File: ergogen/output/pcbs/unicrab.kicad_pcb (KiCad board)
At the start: 2 copper layers, 230 x 104.3 mm, 72 parts

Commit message: update the kicad file
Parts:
- moved T1 46.8 mm to (172.2, 111.0), turned to 0 degrees
- moved B1 38.6 mm to (159.2, 121.0), turned to 90 degrees
- moved JST1 28.3 mm to (187.2, 151.3), turned to -90 degrees
- moved MCU1 2.48 mm to (172.2, 126.4)
- moved D22 1.97 mm to (251.8, 104.1)
- moved D26 1.97 mm to (228.8, 87.7)
- moved S23 1.97 mm to (246.1, 82.8)
- moved S18 1.97 mm to (275.6, 123.1)
- moved S24 1.97 mm to (236.3, 115.7)
- moved D17 1.97 mm to (144.6, 166.3)
- moved S11 1.97 mm to (128.7, 108.6)
- moved D30 1.97 mm to (204.8, 137.2)
- moved D20 1.97 mm to (268.1, 95.1)
- moved D6 1.97 mm to (97.0, 87.7)
- moved D23 1.97 mm to (247.4, 87.7)
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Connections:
- T1 pad 1: pos -> RAW
- T1 pad 2: RAW -> pos
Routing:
- net P017: track 0.00 -> 21.6 mm
- net P008: track 0.00 -> 21.6 mm
- net P020: track 0.00 -> 21.6 mm
- net P029: track 0.00 -> 21.6 mm
- net P031: track 0.00 -> 21.6 mm
- net P006: track 0.00 -> 21.6 mm
- net P106: track 0.00 -> 8.92 mm
- net P009: track 0.00 -> 8.92 mm
- net mirror_tucky_cluster: track 0.00 -> 4.46 mm
- net mirror_reachy_cluster: track 0.00 -> 4.46 mm
- net tucky_cluster: track 0.00 -> 4.46 mm
- net reachy_cluster: track 0.00 -> 4.46 mm
- net mirror_index_top: track 0.00 -> 4.32 mm
- net mirror_ring_bottom: track 0.00 -> 4.32 mm
- net mirror_ring_home: track 0.00 -> 4.32 mm
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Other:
- board size 230 x 104.3 mm -> 230 x 103.8 mm
- net class Default removed

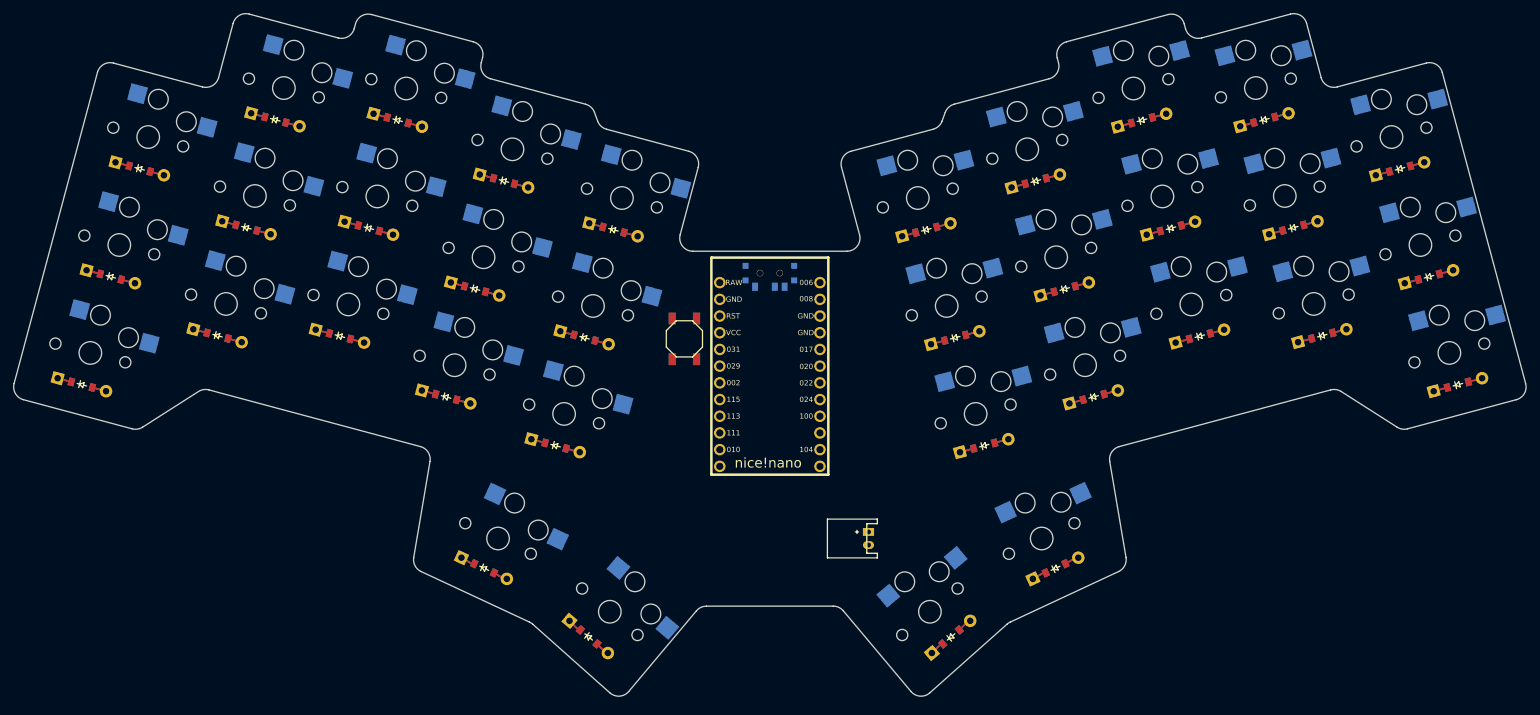
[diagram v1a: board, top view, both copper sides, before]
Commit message: add the pad to diode connections
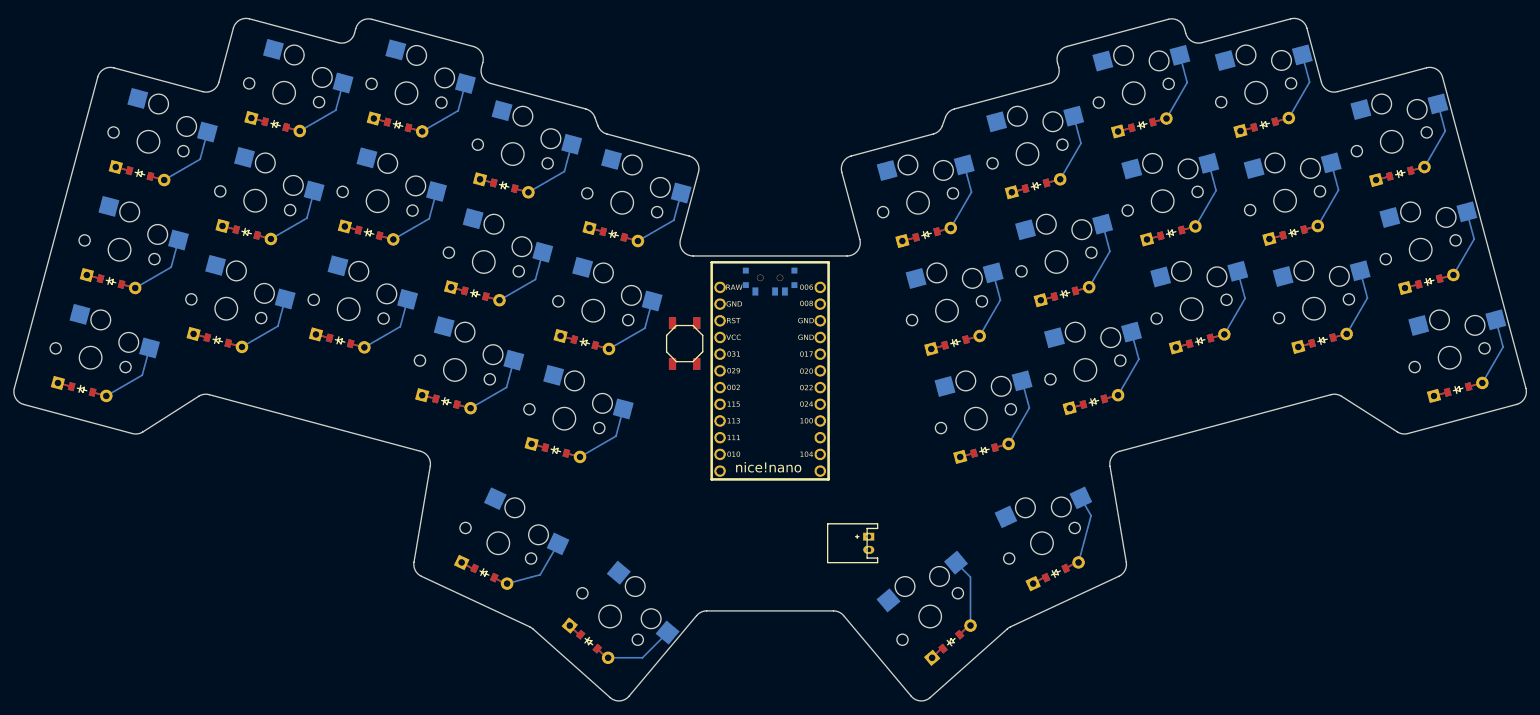
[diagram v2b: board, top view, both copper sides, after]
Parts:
- moved S23 0.72 mm to (246.2, 83.5)
- moved D32 0.72 mm to (196.0, 105.1)
- moved S18 0.72 mm to (275.6, 123.8)
- moved S20 0.72 mm to (266.8, 91.0)
- moved S2 0.72 mm to (73.3, 107.4)
- moved D33 0.72 mm to (215.7, 156.6)
- moved S33 0.72 mm to (213.6, 152.1)
- moved MCU1 0.72 mm to (172.2, 127.1)
- moved D19 0.72 mm to (272.5, 112.3)
- moved D28 0.72 mm to (217.1, 114.1)
- moved D20 0.72 mm to (268.1, 95.8)
- moved S14 0.72 mm to (145.3, 116.7)
- moved S15 0.72 mm to (149.7, 100.3)
- moved S32 0.72 mm to (194.7, 100.3)
- moved S9 0.72 mm to (116.9, 83.6)
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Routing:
- net tucky_cluster: track 4.46 -> 15.1 mm
- net reachy_cluster: track 4.46 -> 15.1 mm
- net inner_top: track 4.32 -> 14.9 mm
- net pinky_bottom: track 4.32 -> 14.9 mm
- net pinky_top: track 4.32 -> 14.9 mm
- net mirror_index_bottom: track 4.32 -> 14.9 mm
- net inner_home: track 4.32 -> 14.9 mm
- net ring_top: track 4.32 -> 14.9 mm
- net index_home: track 4.32 -> 14.9 mm
- net ring_bottom: track 4.32 -> 14.9 mm
- net index_bottom: track 4.32 -> 14.9 mm
- net middle_home: track 4.32 -> 14.9 mm
- net mirror_middle_bottom: track 4.32 -> 14.9 mm
- net middle_bottom: track 4.32 -> 14.9 mm
- net mirror_pinky_bottom: track 4.32 -> 14.9 mm
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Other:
- outline, holes or cut-outs redrawn

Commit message: connect rows and columns
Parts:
- moved D3 3.49 mm to (73.1, 97.0)
- moved S25 3.49 mm to (228.7, 101.2)
- moved D23 3.49 mm to (244.2, 89.5)
- moved D13 3.49 mm to (136.4, 139.1)
- moved S29 3.49 mm to (208.1, 94.0)
- moved S13 3.49 mm to (137.6, 134.3)
- moved D29 3.49 mm to (209.4, 98.8)
- moved S15 3.49 mm to (146.4, 101.4)
- moved D15 3.49 mm to (145.2, 106.2)
- moved D17 3.49 mm to (141.4, 168.2)
- moved D6 3.49 mm to (93.7, 89.5)
- moved S19 3.49 mm to (267.9, 108.6)
- moved D11 3.49 mm to (124.1, 115.3)
- moved D7 3.49 mm to (103.5, 122.4)
- moved D10 3.49 mm to (119.7, 131.7)
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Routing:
- net P002: track 0.00 -> 73.8 mm
- net P010: track 0.00 -> 73.8 mm
- net P115: track 0.00 -> 73.8 mm
- net P111: track 0.00 -> 73.8 mm
- net P113: track 0.00 -> 73.8 mm
- net P017: track 21.6 -> 95.3 mm
- net P008: track 21.6 -> 95.3 mm
- net P029: track 21.6 -> 95.3 mm
- net P006: track 21.6 -> 95.3 mm
- net P020: track 21.6 -> 95.3 mm
- net P031: track 21.6 -> 78.3 mm
- net P106: track 8.92 -> 27.6 mm
- net P009: track 8.92 -> 27.4 mm
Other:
- outline, holes or cut-outs redrawn

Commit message: add reset and switch connection
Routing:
- net GND: track 0.00 -> 14.6 mm
- net RST: track 0.00 -> 9.88 mm
- net RAW: track 0.00 -> 5.63 mm
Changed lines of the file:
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@@
 		(net 47)
 	)
+	(segment
+		(start 161.949416 114.91072)
+		(end 161.325164 114.286468)
+		(width 0.25)
+		(layer "B.Cu")
+		(net 48)
+	)
+	(segment
+		(start 166.695165 114.91072)
+		(end 161.949416 114.91072)
+		(width 0.25)
+		(layer "B.Cu")
+		(net 48)
+	)
+	(segment
+		(start 154.095161 119.73572)
+		(end 154.095161 125.935726)
+		(width 0.25)
+		(layer "F.Cu")
+		(net 50)
+	)
+	(segment
+		(start 157.004413 116.826468)
+		(end 161.325164 116.826468)
+		(width 0.25)
+		(layer "F.Cu")
+		(net 50)
+	)
+	(segment
+		(start 154.095161 119.73572)
+		(end 157.004413 116.826468)
+		(width 0.25)
+		(layer "F.Cu")
+		(net 50)
+	)
+	(segment
+		(start 160.955912 119.73572)
+		(end 161.325164 119.366468)
+		(width 0.25)
+		(layer "F.Cu")
+		(net 51)
+	)
+	(segment
+		(start 157.795161 119.73572)
+		(end 157.795161 125.935726)
+		(width 0.25)
+		(layer "F.Cu")
+		(net 51)
+	)
+	(segment
+		(start 157.795161 119.73572)
+		(end 160.955912 119.73572)
+		(width 0.25)
+		(layer "F.Cu")
+		(net 51)
+	)
 )

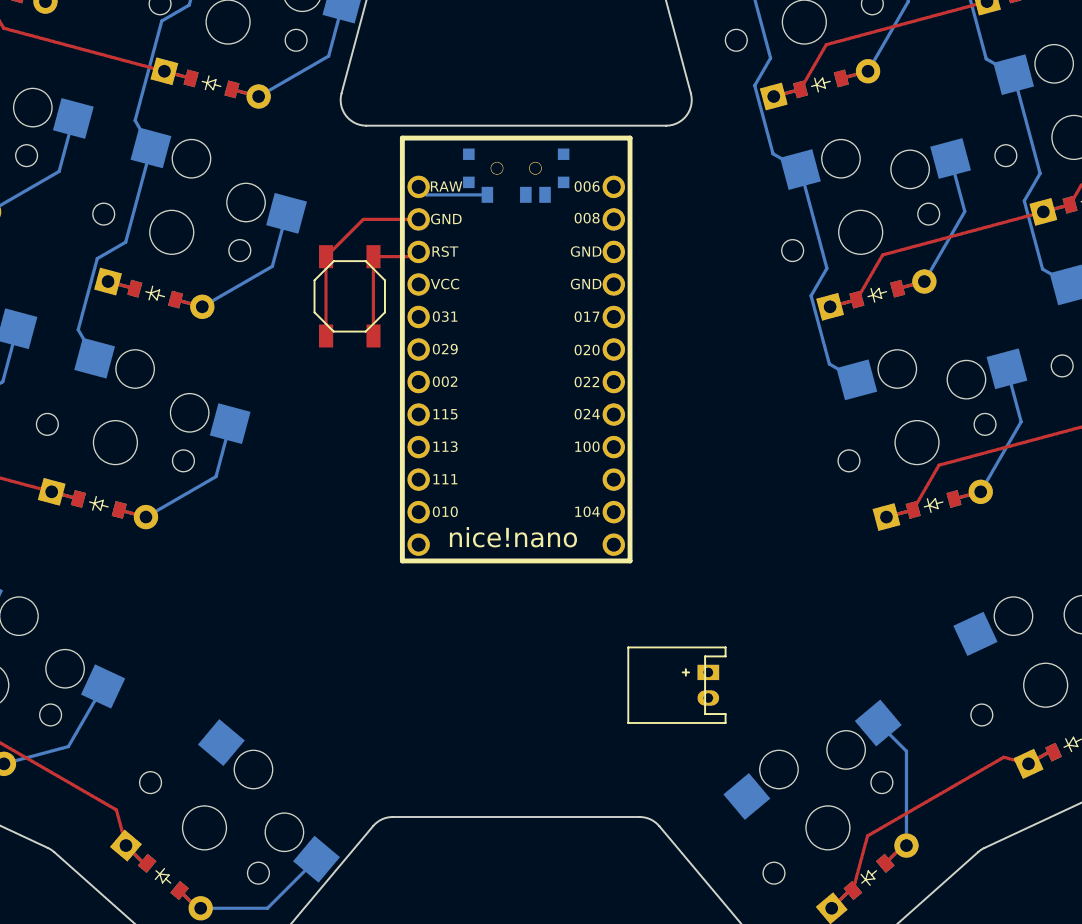
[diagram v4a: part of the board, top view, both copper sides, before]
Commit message: connect the rows
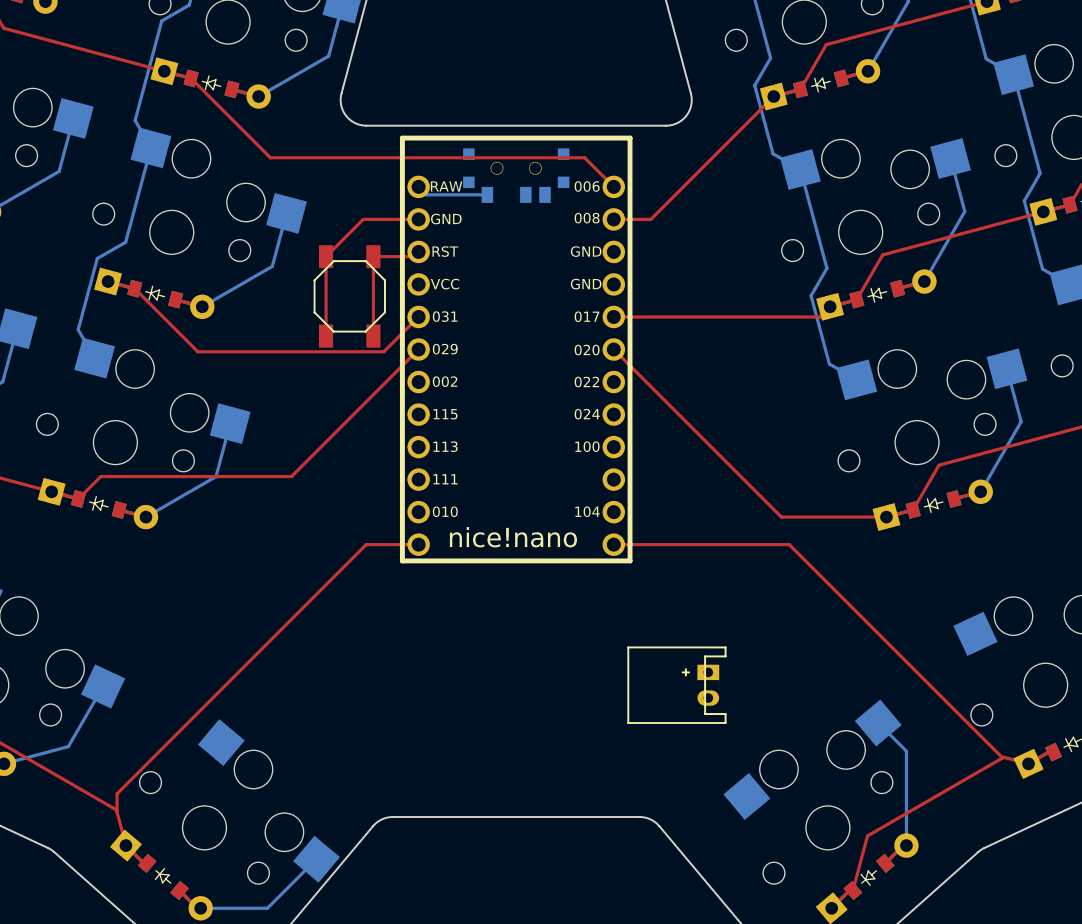
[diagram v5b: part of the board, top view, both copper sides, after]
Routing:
- net P106: track 27.6 -> 64.9 mm
- net P006: track 95.3 -> 131.8 mm
- net P009: track 27.4 -> 60.4 mm
- net P029: track 95.3 -> 126.7 mm
- net P020: track 95.3 -> 122.0 mm
- net P031: track 78.3 -> 103.7 mm
- net P017: track 95.3 -> 112.5 mm
- net P008: track 95.3 -> 111.7 mm
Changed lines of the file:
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@@
+	)
+	(segment
+		(start 134.75744 138.659044)
+		(end 136.510617 136.905867)
+		(width 0.25)
+		(layer "F.Cu")
+		(net 40)
 	)
 	(segment
@@
 	)
 	(segment
+		(start 136.510617 136.905867)
+		(end 151.405765 136.905867)
+		(width 0.25)
+		(layer "F.Cu")
+		(net 40)
+	)
+	(segment
 		(start 74.310502 125.376632)
 		(end 81.248683 121.370873)
@@
 	)
 	(segment
+		(start 151.405765 136.905867)
+		(end 161.325164 126.986468)
+		(width 0.25)
+		(layer "F.Cu")
+		(net 40)
+	)
+	(segment
 		(start 132.671041 138.099991)
 		(end 134.757442 138.659036)
@@
 	)
 	(segment
+		(start 144.079783 127.160726)
+		(end 158.610905 127.160726)
+		(width 0.25)
+		(layer "F.Cu")
+		(net 41)
+	)
+	(segment
 		(start 87.735003 105.509184)
 		(end 92.357308 102.840495)
@@
 	)
 	(segment
+		(start 139.157363 122.238306)
+		(end 144.079783 127.160726)
+		(width 0.25)
+		(layer "F.Cu")
+		(net 41)
+	)
+	(segment
 		(start 67.102749 112.963151)
 		(end 67.141572 112.818263)
@@
 	)
 	(segment
+		(start 158.610905 127.160726)
+		(end 161.325164 124.446467)
+		(width 0.25)
+		(layer "F.Cu")
+		(net 41)
+	)
+	(segment
 		(start 106.351059 105.579781)
 		(end 109.709816 111.397317)
@@
 	)
 	(segment
+		(start 149.750445 112.010721)
+		(end 174.289417 112.010721)
+		(width 0.25)
+		(layer "F.Cu")
+		(net 42)
+	)
+	(segment
 		(start 128.923513 101.896452)
 		(end 126.908258 98.405931)
@@
 	)
 	(segment
+		(start 174.289417 112.010721)
+		(end 176.565164 114.286468)
+		(width 0.25)
+		(layer "F.Cu")
+		(net 42)
+	)
+	(segment
 		(start 141.470888 105.258512)
 		(end 128.923513 101.896452)
@@
 	)
 	(segment
+		(start 143.557286 105.817562)
+		(end 149.750445 112.010721)
+		(width 0.25)
+		(layer "F.Cu")
+		(net 42)
+	)
+	(segment
 		(start 71.502671 96.54241)
 		(end 71.502674 96.542417)
@@
 	)
 	(segment
+		(start 137.779662 163.15)
+		(end 138.469497 165.724506)
+		(width 0.25)
+		(layer "F.Cu")
+		(net 43)
+	)
+	(segment
 		(start 123.991051 157.0362)
 		(end 126.3862 156.394421)
@@
 	)
 	(segment
+		(start 161.325164 142.226468)
+		(end 157.236649 142.226468)
+		(width 0.25)
+		(layer "F.Cu")
+		(net 43)
+	)
+	(segment
 		(start 122.033428 156.123345)
 		(end 123.733892 157.105111)
@@
 	)
 	(segment
+		(start 157.236649 142.226468)
+		(end 137.779662 161.683455)
+		(width 0.25)
+		(layer "F.Cu")
+		(net 43)
+	)
+	(segment
 		(start 126.3862 156.394421)
 		(end 137.723377 162.939942)
@@
 	)
 	(segment
+		(start 137.779662 161.683455)
+		(end 137.779662 163.15)
+		(width 0.25)
+		(layer "F.Cu")
+		(net 43)
+	)
+	(segment
 		(start 137.723377 162.939942)
-		(end 138.469497 165.724506)
+		(end 137.779662 163.15)
 		(width 0.25)
 		(layer "F.Cu")
@@
 	)
 	(segment
+		(start 197.858922 140.072194)
+		(end 189.65089 140.072194)
+		(width 0.25)
+		(layer "F.Cu")
+		(net 44)
+	)
+	(segment
 		(start 230.665233 123.413675)
 		(end 228.209804 127.666601)
@@
 	)
 	(segment
+		(start 189.65089 140.072194)
+		(end 176.565164 126.986468)
+		(width 0.25)
+		(layer "F.Cu")
+		(net 44)
+	)
+	(segment
 		(start 201.960572 136.022628)
 		(end 199.945323 139.513144)
@@
 	)
 	(segment
+		(start 193.459004 123.651454)
+		(end 192.663991 124.446467)
+		(width 0.25)
+		(layer "F.Cu")
+		(net 45)
+	)
+	(segment
 		(start 246.967758 106.36329)
 		(end 246.96776 106.363287)
@@
 	)
 	(segment
+		(start 192.663991 124.446467)
+		(end 176.565164 124.446467)
+		(width 0.25)
+		(layer "F.Cu")
+		(net 45)
+	)
+	(segment
 		(start 254.775506 110.871094)
 		(end 246.967759 106.363291)
@@
 	)
 	(segment
+		(start 189.059078 107.230719)
+		(end 179.463329 116.826468)
+		(width 0.25)
+		(layer "F.Cu")
+		(net 46)
+	)
+	(segment
 		(start 189.059077 107.230717)
 		(end 191.145475 106.671672)
@@
 	)
 	(segment
+		(start 179.463329 116.826468)
+		(end 176.565164 116.826468)
+		(width 0.25)
+		(layer "F.Cu")
+		(net 46)
+	)
+	(segment
 		(start 263.200096 97.396516)
 		(end 263.200096 97.396516)
@@
 	)
 	(segment
+		(start 206.916857 158.870844)
+		(end 206.945844 158.870844)
+		(width 0.25)
+		(layer "F.Cu")
+		(net 47)
+	)
+	(segment
 		(start 210.651294 158.361931)
 		(end 210.908454 158.430841)
@@
 	)
 	(segment
+		(start 207.022006 158.826872)
+		(end 206.945844 158.870844)
+		(width 0.25)
+		(layer "F.Cu")
+		(net 47)
+	)
+	(segment
 		(start 208.95083 159.343699)
 		(end 210.651294 158.361931)
@@
 	)
 	(segment
+		(start 190.272481 142.226468)
+		(end 206.916857 158.870844)
+		(width 0.25)
+		(layer "F.Cu")
+		(net 47)
+	)
+	(segment
+		(start 176.565164 142.226468)
+		(end 190.272481 142.226468)
+		(width 0.25)
+		(layer "F.Cu")
+		(net 47)
+	)
+	(segment
 		(start 196.380611 164.970684)
 		(end 195.238223 169.23413)
@@
 	)
 	(segment
+		(start 206.945844 158.870844)
+		(end 196.380611 164.970684)
+		(width 0.25)
+		(layer "F.Cu")
+		(net 47)
+	)
+	(segment
 		(start 193.583568 170.622555)
 		(end 194.97199 169.234128)
 		(width 0.25)
 		(layer "F.Cu")
-		(net 47)
-	)
-	(segment
-		(start 207.022006 158.826872)
-		(end 196.380611 164.970684)
-		(width 0.25)
-		(layer "F.Cu")

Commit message: connect the battery
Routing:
- net GND: track 14.6 -> 95.0 mm
- net pos: track 0.00 -> 43.2 mm, vias 0 -> 1
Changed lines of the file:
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@@
+	)
+	(segment
+		(start 169.675 137.931827)
+		(end 183.945161 152.201988)
+		(width 0.25)
+		(layer "F.Cu")
+		(net 49)
+	)
+	(segment
+		(start 169.675 122.65)
+		(end 169.675 137.931827)
+		(width 0.25)
+		(layer "F.Cu")
+		(net 49)
+	)
+	(via
+		(at 169.675 122.65)
+		(size 0.8)
+		(drill 0.4)
+		(layers "F.Cu" "B.Cu")
+		(net 49)
+	)
+	(segment
+		(start 169.695165 122.629835)
+		(end 169.675 122.65)
+		(width 0.25)
+		(layer "B.Cu")
+		(net 49)
+	)
+	(segment
+		(start 169.695165 114.910721)
+		(end 169.695165 122.629835)
+		(width 0.25)
+		(layer "B.Cu")
+		(net 49)
+	)
+	(segment
+		(start 169.225 139.481827)
+		(end 183.945161 154.201988)
+		(width 0.25)
+		(layer "F.Cu")
+		(net 50)
 	)
 	(segment
 		(start 154.095161 119.73572)
 		(end 154.095161 125.935726)
+		(width 0.25)
+		(layer "F.Cu")
+		(net 50)
+	)
+	(segment
+		(start 161.325164 116.826468)
+		(end 169.225 124.726304)
+		(width 0.25)
+		(layer "F.Cu")
+		(net 50)
+	)
+	(segment
+		(start 163.865164 119.366468)
+		(end 176.565164 119.366468)
+		(width 0.25)
+		(layer "F.Cu")
+		(net 50)
+	)
+	(segment
+		(start 161.325164 116.826468)
+		(end 163.865164 119.366468)
 		(width 0.25)
 		(layer "F.Cu")
@@
 		(width 0.25)
 		(layer "F.Cu")
+		(net 50)
+	)
+	(segment
+		(start 169.225 124.726304)
+		(end 169.225 139.481827)
+		(width 0.25)
+		(layer "F.Cu")
+		(net 50)
+	)
+	(segment
+		(start 166.405164 121.906468)
+		(end 161.325164 116.826468)
+		(width 0.25)
+		(layer "F.Cu")
+		(net 50)
+	)
+	(segment
+		(start 176.565164 121.906468)
+		(end 166.405164 121.906468)
+		(width 0.25)
+		(layer "F.Cu")

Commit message: finish connectionx
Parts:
- moved D11 6.16 mm to (118.0, 114.5)
- moved T1 6.16 mm to (162.8, 112.0)
- moved S32 6.16 mm to (185.3, 100.6)
- moved D26 6.16 mm to (219.4, 88.8)
- moved S29 6.16 mm to (202.0, 93.2)
- moved D16 6.16 mm to (119.4, 156.9)
- moved S11 6.16 mm to (119.3, 109.6)
- moved S6 6.16 mm to (88.9, 83.9)
- moved S26 6.16 mm to (218.1, 84.0)
- moved S2 6.16 mm to (63.9, 107.8)
- moved S25 6.16 mm to (222.5, 100.4)
- moved S21 6.16 mm to (245.6, 116.7)
- moved S20 6.16 mm to (257.4, 91.3)
- moved B1 6.16 mm to (149.8, 122.0)
- moved D19 6.16 mm to (263.1, 112.6)
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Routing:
- net P111: track 73.8 -> 353.8 mm, vias 0 -> 2
- net P010: track 73.8 -> 306.7 mm
- net P113: track 73.8 -> 258.3 mm
- net P115: track 73.8 -> 220.4 mm
- net P002: track 73.8 -> 187.7 mm
- net P031: track 103.7 -> 120.7 mm
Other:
- outline, holes or cut-outs redrawn

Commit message: reset mask clearance
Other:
- rule pad_to_mask_clearance: 0.05 -> 0
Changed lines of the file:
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@@
 	)
 	(setup
-		(pad_to_mask_clearance 0.05)
+		(pad_to_mask_clearance 0)
 		(allow_soldermask_bridges_in_footprints no)
 		(pcbplotparams
@@
 			(outputformat 1)
 			(mirror no)
-			(drillshape 1)
+			(drillshape 0)
 			(scaleselection 1)
 			(outputdirectory "")
